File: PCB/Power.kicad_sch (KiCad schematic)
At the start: 18 parts, among them U5 TPS62933

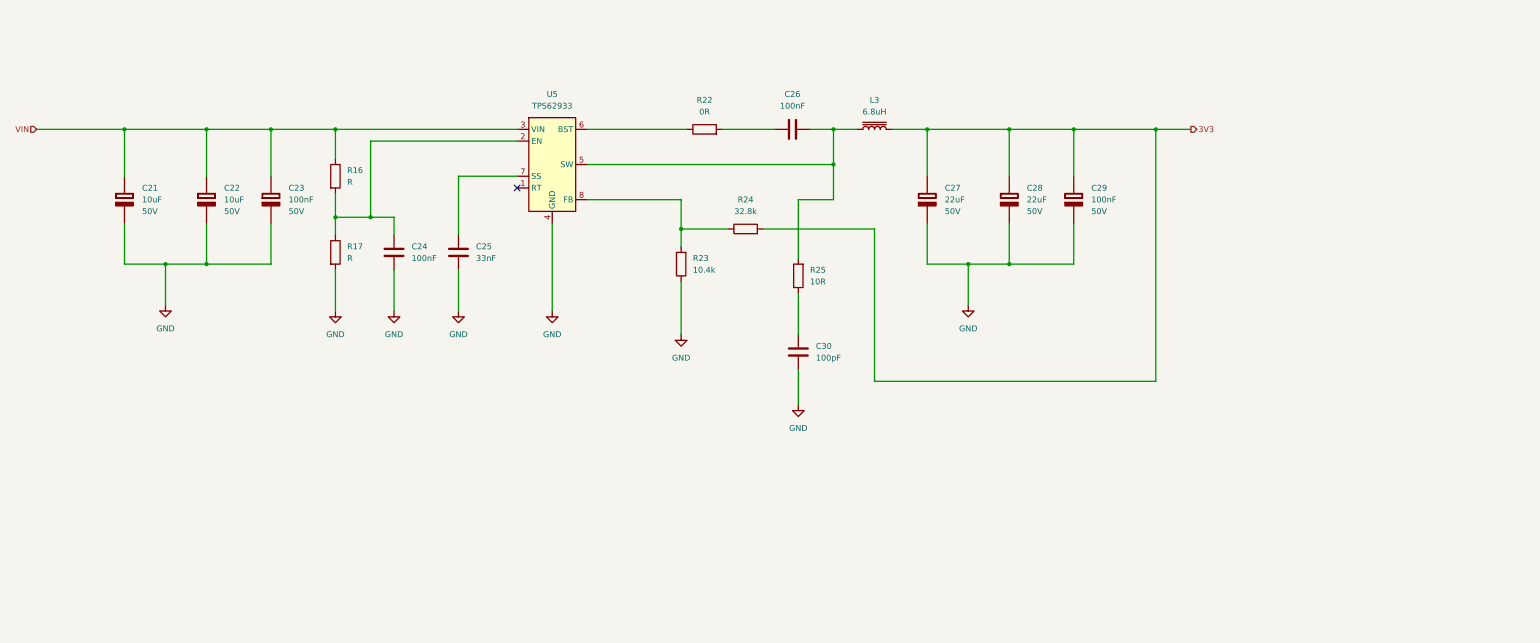
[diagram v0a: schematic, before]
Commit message: Finalized power section schematic
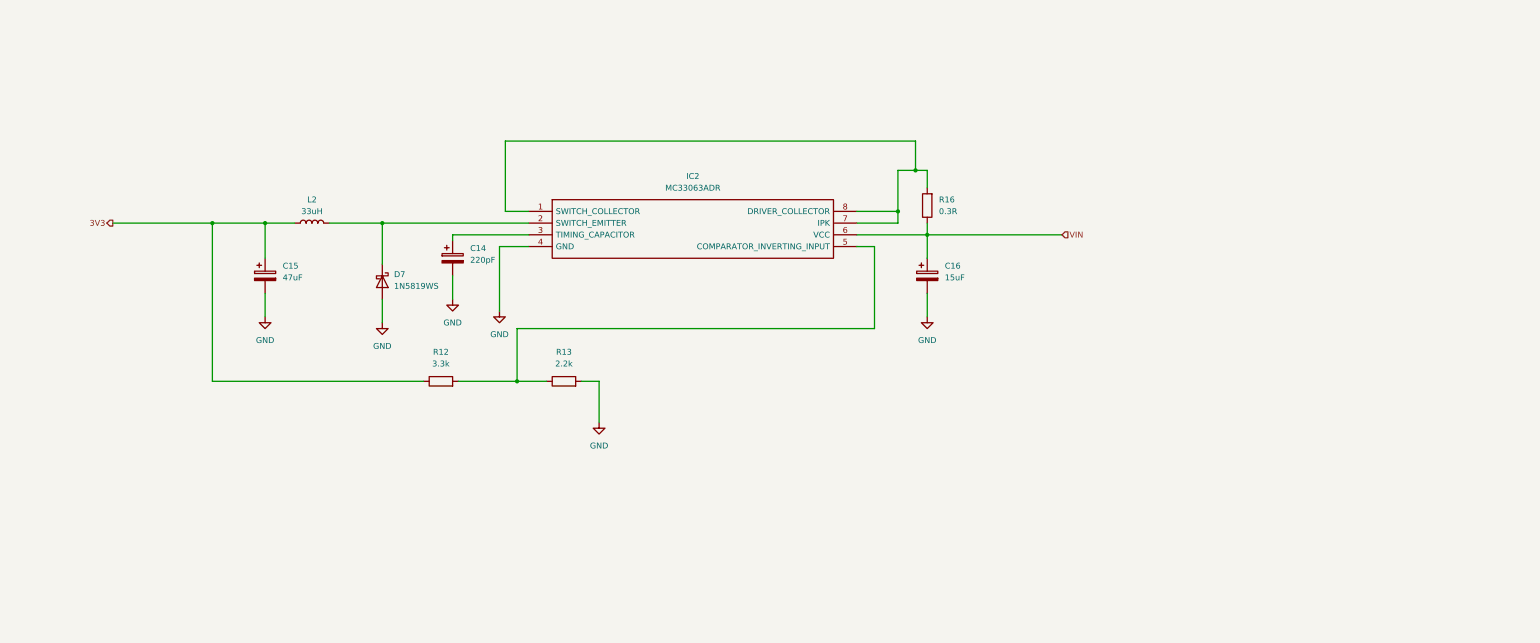
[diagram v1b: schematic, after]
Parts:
- removed C21, C22: 10uF, symbol PCM_Elektuur:C-polar
- removed C23, C29: 100nF, symbol PCM_Elektuur:C-polar
- removed C24, C26: 100nF, symbol Device:C
- removed C25: 33nF, symbol Device:C
- removed C27, C28: 22uF, symbol PCM_Elektuur:C-polar
- removed C30: 100pF, symbol Device:C
- removed L3: 6.8uH, symbol Device:L_Iron
- removed R17: R, symbol Device:R
- removed R22: 0R, symbol Device:R
- removed R23: 10.4k, symbol Device:R
- removed R24: 32.8k, symbol Device:R
- removed R25: 10R, symbol Device:R
- removed U5: TPS62933, Package_TO_SOT_SMD:SOT-583-8, symbol Regulator_Switching:TPS62933
- added C14: 220pF, symbol Device:C_Polarized
- added C15: 47uF, symbol Device:C_Polarized
- added C16: 15uF, symbol Device:C_Polarized
- added D7: 1N5819WS, Diode_SMD:D_SOD-323, symbol Diode:1N5819WS
- added IC2: MC33063ADR, Footprints:SOIC127P600X175-8N, symbol IMU_V100:MC33063ADR
- added L2: 33uH, symbol Device:L
- added R12: 3.3k, symbol Device:R
- added R13: 2.2k, symbol Device:R
- R16: value R -> 0.3R
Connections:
- net 3V3: now also C15.1, L2.1, R12.1
- net GND: now also C14.2, C15.2, C16.2, D7.2 (A), IC2.4 (GND), R13.2
- net VIN: now also C16.1, IC2.6 (VCC)
- net at R16.2: now also IC2.1 (SWITCH_COLLECTOR), IC2.7 (IPK), IC2.8 (DRIVER_COLLECTOR)
- new net: IC2.5 (COMPARATOR_INVERTING_INPUT), R12.2, R13.1
- new net: C14.1, IC2.3 (TIMING_CAPACITOR)
- new net: D7.1 (K), IC2.2 (SWITCH_EMITTER), L2.2
- no-connect marks 1 -> 0

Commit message: Updated PCB
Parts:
- removed C14: 220pF, symbol Device:C_Polarized
- added C21: 75pF, symbol Device:C
- added C22: 1nF, symbol Device:C
- C15: value 47uF -> 470uF
- C16: value 15uF -> 100uF
- L2: value 33uH -> 470uH
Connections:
- net 3V3: now also C22.1
- net GND: now also C21.2, C22.2
- net at IC2.3 (TIMING_CAPACITOR): now also C21.1
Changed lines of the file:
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@@
 	)
 	(junction
-		(at 63.5 87.63)
+		(at 46.99 87.63)
 		(diameter 0)
 		(color 0 0 0 0)
@@
 		(color 0 0 0 0)
 	)
+	(junction
+		(at 60.96 87.63)
+		(diameter 0)
+		(color 0 0 0 0)
+	)
+	(bus_entry
+		(at 346.71 173.99)
+		(size 2.54 2.54)
+		(stroke
+			(width 0)
+			(type default)
+		)
+	)
 	(wire
 		(pts
@@
 	(wire
 		(pts
-			(xy 109.22 121.92) (xy 63.5 121.92)
+			(xy 109.22 121.92) (xy 46.99 121.92)
 		)
 		(stroke
@@
 	(wire
 		(pts
-			(xy 63.5 121.92) (xy 63.5 87.63)
+			(xy 46.99 121.92) (xy 46.99 87.63)
 		)
 		(stroke
@@
 	(wire
 		(pts
+			(xy 60.96 102.87) (xy 60.96 107.95)
+		)
+		(stroke
+			(width 0)
+			(type default)
+		)
+	)
+	(wire
+		(pts
 			(xy 203.2 87.63) (xy 212.09 87.63)
 		)
@@
 	(wire
 		(pts
+			(xy 60.96 87.63) (xy 60.96 95.25)
+		)
+		(stroke
+			(width 0)
+			(type default)
+		)
+	)
+	(wire
+		(pts
 			(xy 74.93 102.87) (xy 74.93 107.95)
 		)
@@
 	(wire
 		(pts
-			(xy 41.91 87.63) (xy 63.5 87.63)
+			(xy 25.4 87.63) (xy 46.99 87.63)
 		)
 		(stroke
@@
 	(wire
 		(pts
+			(xy 60.96 87.63) (xy 74.93 87.63)
+		)
+		(stroke
+			(width 0)
+			(type default)
+		)
+	)
+	(wire
+		(pts
 			(xy 212.09 87.63) (xy 212.09 85.09)
 		)
@@
 	(wire
 		(pts
-			(xy 63.5 87.63) (xy 74.93 87.63)
+			(xy 46.99 87.63) (xy 60.96 87.63)
 		)
 		(stroke
@@
 	(hierarchical_label "3V3"
 		(shape output)
-		(at 41.91 87.63 180)
+		(at 25.4 87.63 180)
 		(effects
 			(font
@@
 			)
 			(justify right)
+		)
+	)
+	(symbol
+		(lib_id "Device:C")
+		(at 60.96 99.06 0)
+		(unit 1)
+		(exclude_from_sim no)
+		(in_bom yes)
+		(on_board yes)
+		(dnp no)
+		(fields_autoplaced yes)
+		(property "Reference" "C22"
+			(at 64.77 97.7899 0)
+			(effects
+				(font
+					(size 1.27 1.27)
+				)
+				(justify left)
+			)
+		)
+		(property "Value" "1nF"
+			(at 64.77 100.3299 0)
+			(effects
+				(font
+					(size 1.27 1.27)
+				)
+				(justify left)
+			)
+		)
+		(property "Footprint" ""
+			(at 61.9252 102.87 0)
+			(effects
+				(font
+					(size 1.27 1.27)
+				)
+				(hide yes)
+			)
+		)
+		(property "Datasheet" "~"
+			(at 60.96 99.06 0)
+			(effects
+				(font
+					(size 1.27 1.27)
+				)
+				(hide yes)
+			)
+		)
+		(property "Description" "Unpolarized capacitor"
+			(at 60.96 99.06 0)
+			(effects
+				(font
+					(size 1.27 1.27)
+				)
+				(hide yes)
+			)
+		)
+		(pin "2"
+		)
+		(pin "1"
+		)
+		(instances
+			(project "IMU_V100"
+				(path "/b6a8d14b-6e32-4628-bf0c-2046877d1cfa/205555cc-3b86-4915-975e-3a7e3eed6661/f9424131-b250-4638-a784-b5462b05c1af"
+					(reference "C22")
+					(unit 1)
+				)
+			)
 		)
 	)
@@
 			)
 		)
-		(property "Value" "47uF"
+		(property "Value" "470uF"
 			(at 78.74 99.4409 0)
 			(effects
@@
 				(path "/b6a8d14b-6e32-4628-bf0c-2046877d1cfa/205555cc-3b86-4915-975e-3a7e3eed6661/f9424131-b250-4638-a784-b5462b05c1af"
 					(reference "C15")
+					(unit 1)
+				)
+			)
+		)
+	)
+	(symbol
+		(lib_id "power:GND")
+		(at 60.96 107.95 0)
+		(unit 1)
+		(exclude_from_sim no)
+		(in_bom yes)
+		(on_board yes)
+		(dnp no)
+		(fields_autoplaced yes)
+		(property "Reference" "#PWR036"
+			(at 60.96 114.3 0)
+			(effects
+				(font
+					(size 1.27 1.27)
+				)
+				(hide yes)
+			)
+		)
+		(property "Value" "GND"
+			(at 60.96 113.03 0)
+			(effects
+				(font
+					(size 1.27 1.27)
+				)
+			)
+		)
+		(property "Footprint" ""
+			(at 60.96 107.95 0)
+			(effects
+				(font
+					(size 1.27 1.27)
+				)
+				(hide yes)
+			)
+		)
+		(property "Datasheet" ""
+			(at 60.96 107.95 0)
+			(effects
+				(font
+					(size 1.27 1.27)
+				)
+				(hide yes)
+			)
+		)
+		(property "Description" "Power symbol creates a global label with name \"GND\" , ground"
+			(at 60.96 107.95 0)
+			(effects
+				(font
+					(size 1.27 1.27)
+				)
+				(hide yes)
+			)
+		)
+		(pin "1"
+		)
+		(instances
+			(project "IMU_V100"
+				(path "/b6a8d14b-6e32-4628-bf0c-2046877d1cfa/205555cc-3b86-4915-975e-3a7e3eed6661/f9424131-b250-4638-a784-b5462b05c1af"
+					(reference "#PWR036")
 					(unit 1)
 				)
@@
 	)
 	(symbol
-		(lib_id "Device:C_Polarized")
-		(at 115.57 95.25 0)
-		(unit 1)
-		(exclude_from_sim no)
-		(in_bom yes)
-		(on_board yes)
-		(dnp no)
-		(fields_autoplaced yes)
-		(property "Reference" "C14"
-			(at 119.38 93.0909 0)
-			(effects
-				(font
-					(size 1.27 1.27)
-				)
-				(justify left)
-			)
-		)
-		(property "Value" "220pF"
-			(at 119.38 95.6309 0)
-			(effects
-				(font
-					(size 1.27 1.27)
-				)
-				(justify left)
-			)
-		)
-		(property "Footprint" ""
-			(at 116.5352 99.06 0)
-			(effects
-				(font
-					(size 1.27 1.27)
-				)
-				(hide yes)
-			)
-		)
-		(property "Datasheet" "~"
-			(at 115.57 95.25 0)
-			(effects
-				(font
-					(size 1.27 1.27)
-				)
-				(hide yes)
-			)
-		)
-		(property "Description" "Polarized capacitor"
-			(at 115.57 95.25 0)
-			(effects
-				(font
-					(size 1.27 1.27)
-				)
-				(hide yes)
-			)
-		)
-		(pin "1"
-		)
-		(pin "2"
-		)
-		(instances
-			(project ""
-				(path "/b6a8d14b-6e32-4628-bf0c-2046877d1cfa/205555cc-3b86-4915-975e-3a7e3eed6661/f9424131-b250-4638-a784-b5462b05c1af"
-					(reference "C14")
-					(unit 1)
-				)
-			)
-		)
-	)
-	(symbol
 		(lib_id "Device:R")
 		(at 139.7 121.92 90)
@@
 			)
 		)
-		(property "Value" "33uH"
+		(property "Value" "470uH"
 			(at 85.09 85.09 90)
 			(effects
@@
 				(path "/b6a8d14b-6e32-4628-bf0c-2046877d1cfa/205555cc-3b86-4915-975e-3a7e3eed6661/f9424131-b250-4638-a784-b5462b05c1af"
 					(reference "L2")
+					(unit 1)
+				)
+			)
+		)
+	)
+	(symbol
+		(lib_id "Device:C")
+		(at 115.57 95.25 0)
+		(unit 1)
+		(exclude_from_sim no)
+		(in_bom yes)
+		(on_board yes)
+		(dnp no)
+		(fields_autoplaced yes)
+		(property "Reference" "C21"
+			(at 119.38 93.9799 0)
+			(effects
+				(font
+					(size 1.27 1.27)
+				)
+				(justify left)
+			)
+		)
+		(property "Value" "75pF"
+			(at 119.38 96.5199 0)
+			(effects
+				(font
+					(size 1.27 1.27)
+				)
+				(justify left)
+			)
+		)
+		(property "Footprint" ""
+			(at 116.5352 99.06 0)
+			(effects
+				(font
+					(size 1.27 1.27)
+				)
+				(hide yes)
+			)
+		)
+		(property "Datasheet" "~"
+			(at 115.57 95.25 0)
+			(effects
+				(font
+					(size 1.27 1.27)
+				)
+				(hide yes)
+			)
+		)
+		(property "Description" "Unpolarized capacitor"
+			(at 115.57 95.25 0)
+			(effects
+				(font
+					(size 1.27 1.27)
+				)
+				(hide yes)
+			)
+		)
+		(pin "2"
+		)
+		(pin "1"
+		)
+		(instances
+			(project ""
+				(path "/b6a8d14b-6e32-4628-bf0c-2046877d1cfa/205555cc-3b86-4915-975e-3a7e3eed6661/f9424131-b250-4638-a784-b5462b05c1af"
+					(reference "C21")
 					(unit 1)
 				)
@@
 			)
 		)
-		(property "Value" "15uF"
+		(property "Value" "100uF"
 			(at 222.25 99.4409 0)
 			(effects

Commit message: Updated PCB
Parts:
- removed C15: 470uF, symbol Device:C_Polarized
- removed C16: 100uF, symbol Device:C_Polarized
- removed C21: 75pF, symbol Device:C
- removed D7: 1N5819WS, Diode_SMD:D_SOD-323, symbol Diode:1N5819WS
- removed IC2: MC33063ADR, Footprints:SOIC127P600X175-8N, symbol IMU_V100:MC33063ADR
- removed R12: 3.3k, symbol Device:R
- removed R13: 2.2k, symbol Device:R
- removed R16: 0.3R, symbol Device:R
- added C17: 560nF, Capacitor_SMD:C_0603_1608Metric, symbol Device:C
- added C18: 4.7uF, Capacitor_SMD:C_0603_1608Metric, symbol Device:C
- added U4: MIC23050-SYML, Package_DFN_QFN:Micrel_MLF-8-1EP_2x2mm_P0.5mm_EP0.6x1.2mm_ThermalVias, symbol Regulator_Switching:MIC23050-SYML
- C16: renamed from C22; value 1nF -> 4.7uF; footprint (none) -> Capacitor_SMD:C_0603_1608Metric
- L2: value 470uH -> 1uH; footprint (none) -> Inductor_SMD:L_0805_2012Metric_Pad1.05x1.20mm_HandSolder
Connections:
- net 3V3: now also L2.2, C17.1, C18.1, U4.4 (SNS); no longer C16.1, L2.1
- net GND: now also C18.2, U4.6 (AGND), U4.8 (PGND), U4.9 (EP_GND)
- net VIN: now also C16.1, U4.2 (EN), U4.7 (VIN)
- new net: L2.1, U4.1 (SW)
- new net CFF: C17.2, U4.5 (CFF)
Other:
- note added: "5V TO 3.3V Converter"
- moved on the sheet: C16
